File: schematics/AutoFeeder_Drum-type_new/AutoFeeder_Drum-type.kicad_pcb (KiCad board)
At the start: 2 copper layers, 68.5 x 80 mm, 58 parts, among them J1 USB_C_Receptacle_6, J2 Conn_01x04, J3 Conn_01x05, J4 Conn_02x02_Odd_Even, J5 Conn_01x04, J6 Conn_01x02, J7 Conn_01x04, J8 Conn_01x03, J9 Conn_01x04, M1 Motor_DC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

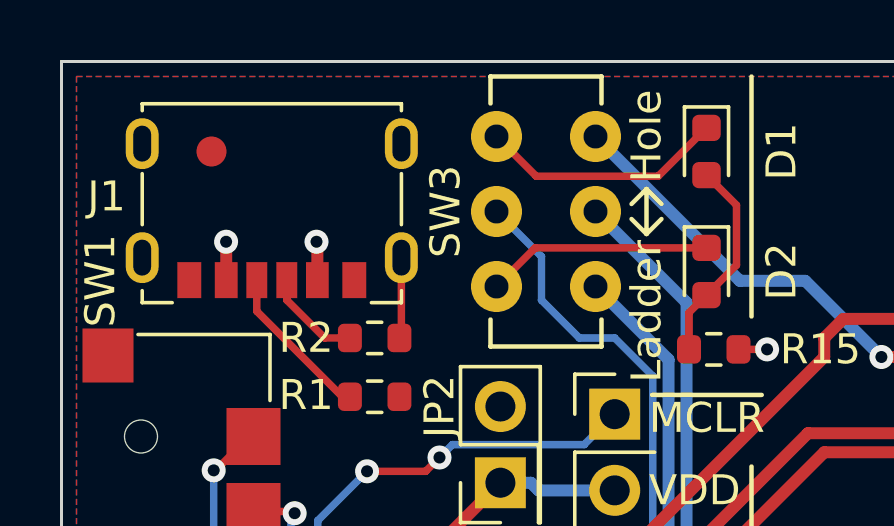
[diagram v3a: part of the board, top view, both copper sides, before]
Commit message: PCB modification: Slightly lengthened the pins of the USB Type-C connector to improve solderability.
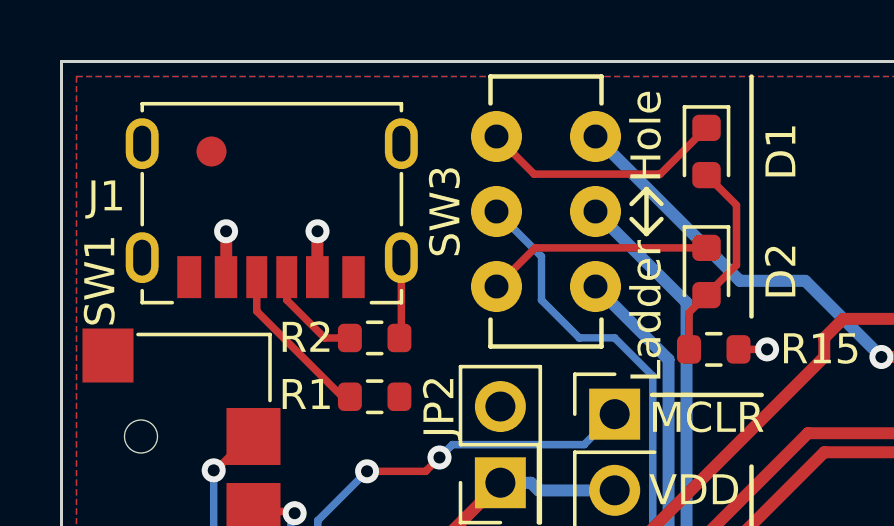
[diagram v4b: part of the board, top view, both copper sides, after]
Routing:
- net +5V: track 49.1 -> 49.8 mm
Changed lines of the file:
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@@
   (net 4 "Net-(J1-PadA5)")
   (net 5 "Net-(J1-PadB5)")
-  (net 6 "Net-(SW3-Pad4)")
+  (net 6 "Net-(D1-Pad1)")
   (net 7 "Net-(D1-Pad2)")
   (net 8 "/Sensor0")
@@
   (net 32 "unconnected-(SW2-Pad5)")
   (net 33 "unconnected-(SW2-Pad6)")
-  (net 34 "Net-(SW3-Pad6)")
+  (net 34 "Net-(D2-Pad1)")
   (net 35 "Net-(J3-Pad4)")
   (net 36 "unconnected-(U1-Pad3)")
@@
     (fp_line (start 4.9 -5.4) (end 4.9 2.6) (layer "F.CrtYd") (width 0.05))
     (fp_line (start 4.9 2.6) (end -4.9 2.6) (layer "F.CrtYd") (width 0.05))
-    (pad "A5" smd rect (at -0.5 -4.55 270) (size 1.2 0.7) (layers "F.Cu" "F.Paste" "F.Mask")
+    (pad "A5" smd rect (at -0.5 -4.45 270) (size 1.4 0.7) (layers "F.Cu" "F.Paste" "F.Mask")
       (net 4 "Net-(J1-PadA5)") (pinfunction "CC1") (pintype "bidirectional"))
-    (pad "A9" smd rect (at 1.52 -4.55 270) (size 1.2 0.76) (layers "F.Cu" "F.Paste" "F.Mask")
+    (pad "A9" smd rect (at 1.525 -4.45 270) (size 1.4 0.75) (layers "F.Cu" "F.Paste" "F.Mask")
       (net 2 "+5V") (pinfunction "VBUS") (pintype "passive"))
-    (pad "A12" smd rect (at 2.75 -4.55 270) (size 1.2 0.8) (layers "F.Cu" "F.Paste" "F.Mask")
+    (pad "A12" smd rect (at 2.75 -4.45 270) (size 1.4 0.8) (layers "F.Cu" "F.Paste" "F.Mask")
       (net 1 "GND") (pinfunction "GND") (pintype "passive"))
-    (pad "B5" smd rect (at 0.5 -4.55 270) (size 1.2 0.7) (layers "F.Cu" "F.Paste" "F.Mask")
+    (pad "B5" smd rect (at 0.5 -4.45 270) (size 1.4 0.7) (layers "F.Cu" "F.Paste" "F.Mask")
       (net 5 "Net-(J1-PadB5)") (pinfunction "CC2") (pintype "bidirectional"))
-    (pad "B9" smd rect (at -1.52 -4.55 270) (size 1.2 0.76) (layers "F.Cu" "F.Paste" "F.Mask")
+    (pad "B9" smd rect (at -1.52 -4.45 270) (size 1.4 0.76) (layers "F.Cu" "F.Paste" "F.Mask")
       (net 2 "+5V") (pinfunction "VBUS") (pintype "passive"))
-    (pad "B12" smd rect (at -2.75 -4.55 270) (size 1.2 0.8) (layers "F.Cu" "F.Paste" "F.Mask")
+    (pad "B12" smd rect (at -2.725 -4.45 270) (size 1.4 0.75) (layers "F.Cu" "F.Paste" "F.Mask")
       (net 1 "GND") (pinfunction "GND") (pintype "passive"))
     (pad "S1" thru_hole oval (at 4.32 -3.8 270) (size 1.7 1.1) (drill oval 1.2 0.6) (layers *.Cu *.Mask)
@@
     (fp_line (start 0.8 -0.4) (end -0.5 -0.4) (layer "F.Fab") (width 0.1))
     (pad "1" smd roundrect (at -0.7875 0 270) (size 0.875 0.95) (layers "F.Cu" "F.Paste" "F.Mask") (roundrect_rratio 0.25)
-      (net 34 "Net-(SW3-Pad6)") (pinfunction "K") (pintype "passive"))
+      (net 34 "Net-(D2-Pad1)") (pinfunction "K") (pintype "passive"))
     (pad "2" smd roundrect (at 0.7875 0 270) (size 0.875 0.95) (layers "F.Cu" "F.Paste" "F.Mask") (roundrect_rratio 0.25)
       (net 7 "Net-(D1-Pad2)") (pinfunction "A") (pintype "passive"))
@@
     (fp_line (start 0.8 0.4) (end 0.8 -0.4) (layer "F.Fab") (width 0.1))
     (pad "1" smd roundrect (at -0.7875 0 270) (size 0.875 0.95) (layers "F.Cu" "F.Paste" "F.Mask") (roundrect_rratio 0.25)
-      (net 6 "Net-(SW3-Pad4)") (pinfunction "K") (pintype "passive"))
+      (net 6 "Net-(D1-Pad1)") (pinfunction "K") (pintype "passive"))
     (pad "2" smd roundrect (at 0.7875 0 270) (size 0.875 0.95) (layers "F.Cu" "F.Paste" "F.Mask") (roundrect_rratio 0.25)
       (net 7 "Net-(D1-Pad2)") (pinfunction "A") (pintype "passive"))
@@
       (net 14 "/Sensor1") (pinfunction "C") (pintype "passive"))
     (pad "4" thru_hole circle locked (at 0 3.3 270) (size 1.7 1.7) (drill 0.8) (layers *.Cu *.Mask)
-      (net 6 "Net-(SW3-Pad4)") (pinfunction "A") (pintype "passive"))
+      (net 6 "Net-(D1-Pad1)") (pinfunction "A") (pintype "passive"))
     (pad "5" thru_hole circle locked (at 2.5 3.3 270) (size 1.7 1.7) (drill 0.8) (layers *.Cu *.Mask)
       (net 35 "Net-(J3-Pad4)") (pinfunction "B") (pintype "passive"))
     (pad "6" thru_hole circle locked (at 5 3.3 270) (size 1.7 1.7) (drill 0.8) (layers *.Cu *.Mask)
-      (net 34 "Net-(SW3-Pad6)") (pinfunction "C") (pintype "passive"))
+      (net 34 "Net-(D2-Pad1)") (pinfunction "C") (pintype "passive"))
   )
   (footprint "Resistor_SMD:R_0603_1608Metric" (layer "F.Cu")
@@
   (segment (start 176.5 109.8) (end 176.2 109.8) (width 0.25) (layer "B.Cu") (net 1))
   (segment (start 176.2 109.8) (end 175 111) (width 0.25) (layer "B.Cu") (net 1))
-  (segment (start 141.99 66.012) (end 141.99 67.288) (width 0.4) (layer "F.Cu") (net 2))
+  (segment (start 145.034 65.659) (end 145.03 65.663) (width 0.4) (layer "F.Cu") (net 2))
   (segment (start 156.4 98.425) (end 155.765 97.79) (width 0.25) (layer "F.Cu") (net 2))
+  (segment (start 145.03 65.663) (end 145.03 67.288) (width 0.4) (layer "F.Cu") (net 2))
   (segment (start 156.718 117.983) (end 155.478 117.983) (width 0.4) (layer "F.Cu") (net 2))
   (segment (start 185.98 68.505) (end 186.88 69.405) (width 0.4) (layer "F.Cu") (net 2))
@@
   (segment (start 185.98 61.585) (end 185.98 68.505) (width 0.25) (layer "F.Cu") (net 2))
   (segment (start 186.88 69.405) (end 186.88 73) (width 0.4) (layer "F.Cu") (net 2))
-  (segment (start 145 66.008) (end 145.03 66.038) (width 0.4) (layer "F.Cu") (net 2))
   (segment (start 156.21 100.19) (end 155.38 100.19) (width 0.25) (layer "F.Cu") (net 2))
   (segment (start 186.215 61.35) (end 185.98 61.585) (width 0.25) (layer "F.Cu") (net 2))
@@
   (segment (start 155.38 100.19) (end 155.38 104.5) (width 0.25) (layer "F.Cu") (net 2))
   (segment (start 156.591 98.425) (end 156.21 98.806) (width 0.25) (layer "F.Cu") (net 2))
-  (segment (start 145.03 66.038) (end 145.03 67.288) (width 0.4) (layer "F.Cu") (net 2))
+  (segment (start 141.986 65.659) (end 141.99 65.663) (width 0.4) (layer "F.Cu") (net 2))
   (segment (start 186.63 61.35) (end 186.215 61.35) (width 0.25) (layer "F.Cu") (net 2))
   (segment (start 156.21 98.806) (end 156.21 100.19) (width 0.25) (layer "F.Cu") (net 2))
   (segment (start 160.02 69.596) (end 159.067 69.596) (width 0.25) (layer "F.Cu") (net 2))
+  (segment (start 141.99 65.663) (end 141.99 67.288) (width 0.4) (layer "F.Cu") (net 2))
   (segment (start 181.685 68.505) (end 185.98 68.505) (width 0.25) (layer "F.Cu") (net 2))
-  (segment (start 141.986 66.008) (end 141.99 66.012) (width 0.4) (layer "F.Cu") (net 2))
   (segment (start 187.185 76) (end 186.88 75.695) (width 0.4) (layer "F.Cu") (net 2))
   (via (at 156.718 117.983) (size 0.8) (drill 0.4) (layers "F.Cu" "B.Cu") (net 2))
@@
   (via (at 181.685 68.505) (size 0.8) (drill 0.4) (layers "F.Cu" "B.Cu") (net 2))
   (via (at 160.02 69.596) (size 0.8) (drill 0.4) (layers "F.Cu" "B.Cu") (net 2))
-  (via (at 145 66.008) (size 0.8) (drill 0.4) (layers "F.Cu" "B.Cu") (net 2))
-  (via (at 141.986 66.008) (size 0.8) (drill 0.4) (layers "F.Cu" "B.Cu") (net 2))
+  (via (at 145.034 65.659) (size 0.8) (drill 0.4) (layers "F.Cu" "B.Cu") (net 2))
+  (via (at 141.986 65.659) (size 0.8) (drill 0.4) (layers "F.Cu" "B.Cu") (net 2))
   (segment (start 176.5 68.5) (end 181.68 68.5) (width 0.25) (layer "B.Cu") (net 2))
   (segment (start 176.5 78) (end 176.5 68.5) (width 0.25) (layer "B.Cu") (net 2))
@@
   (segment (start 145.86 71.175) (end 143.01 68.325) (width 0.25) (layer "F.Cu") (net 5))
   (segment (start 143.01 68.325) (end 143.01 67.288) (width 0.25) (layer "F.Cu") (net 5))
-  (segment (start 152.325 63.825) (end 156.3875 63.825) (width 0.25) (layer "F.Cu") (net 6))
-  (segment (start 156.3875 63.825) (end 158 62.2125) (width 0.25) (layer "F.Cu") (net 6))
-  (segment (start 151 62.5) (end 152.325 63.825) (width 0.25) (layer "F.Cu") (net 6))
+  (segment (start 151 62.5) (end 152.254 63.754) (width 0.25) (layer "F.Cu") (net 6))
+  (segment (start 152.254 63.754) (end 156.4585 63.754) (width 0.25) (layer "F.Cu") (net 6))
+  (segment (start 156.4585 63.754) (end 158 62.2125) (width 0.25) (layer "F.Cu") (net 6))
   (segment (start 157.417 68.3705) (end 157.417 69.596) (width 0.25) (layer "F.Cu") (net 7))
   (segment (start 159 64.7875) (end 159 66.7875) (width 0.25) (layer "F.Cu") (net 7))
@@
   (via (at 141.573397 73.628797) (size 0.8) (drill 0.4) (layers "F.Cu" "B.Cu") (net 30))
   (segment (start 141.573397 83.915397) (end 141.573397 73.628797) (width 0.25) (layer "B.Cu") (net 30))
+  (segment (start 151 67.5) (end 152.2875 66.2125) (width 0.25) (layer "F.Cu") (net 34))
   (segment (start 152.2875 66.2125) (end 158 66.2125) (width 0.25) (layer "F.Cu") (net 34))
-  (segment (start 151 67.5) (end 152.2875 66.2125) (width 0.25) (layer "F.Cu") (net 34))
   (segment (start 151.7 80.645) (end 153.035 80.645) (width 0.25) (layer "F.Cu") (net 35))
   (segment (start 154.305 79.375) (end 154.94 79.375) (width 0.25) (layer "F.Cu") (net 35))

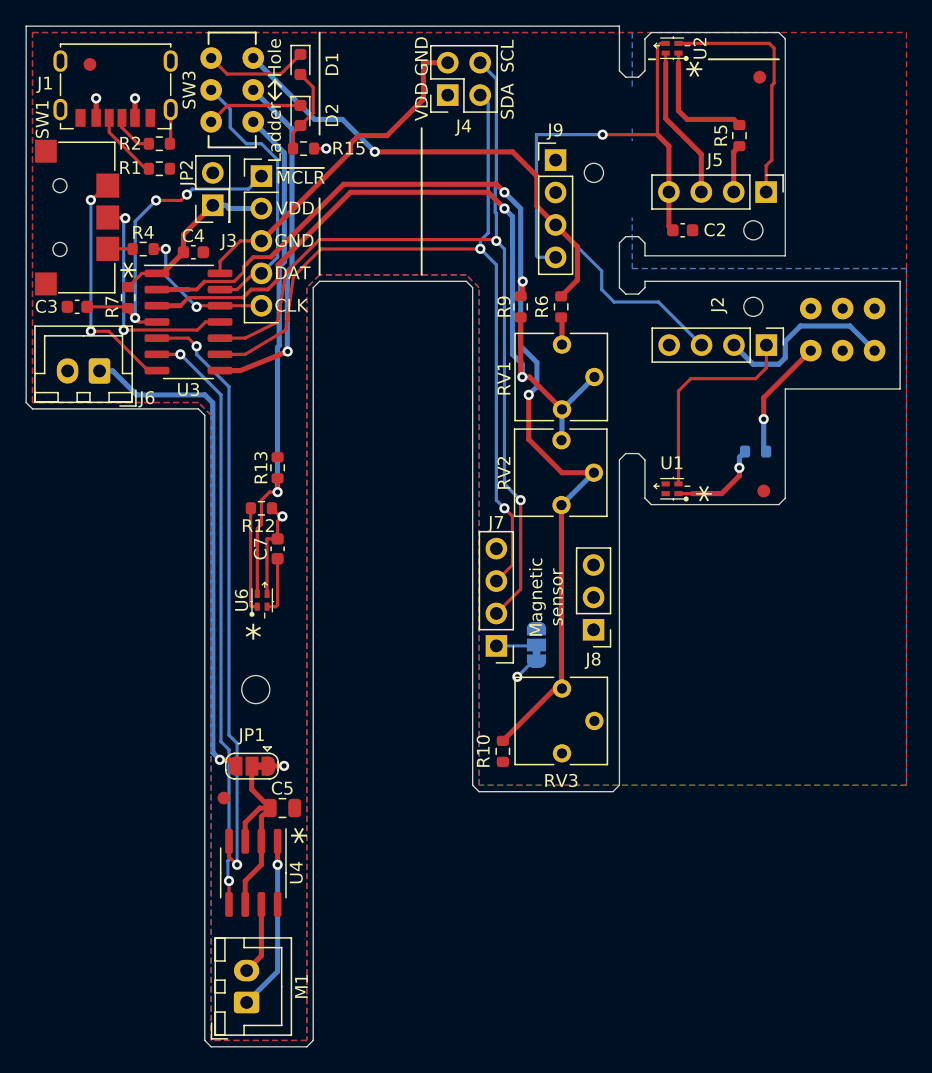
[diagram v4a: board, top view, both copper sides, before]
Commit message: Change schematics: Assign CW/CCW pin to connector; Add M3 mounting hole
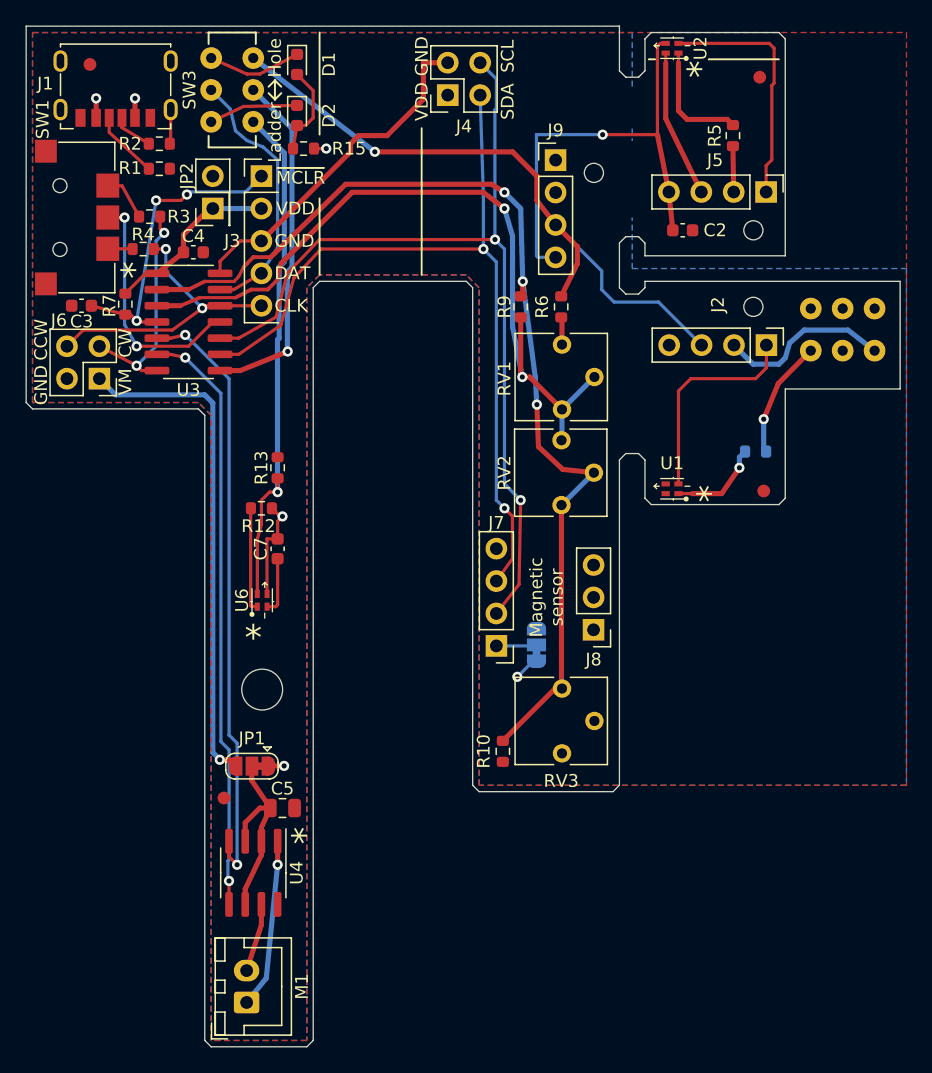
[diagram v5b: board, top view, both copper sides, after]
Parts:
- removed the REF** at (154.5, 112.0)
- added R3: 1k, Resistor_SMD:R_0603_1608Metric, F.Cu at (146.2, 74.9)
- added REF**: MountingHole_3.2mm_M3_DIN965, MountingHole:MountingHole_3.2mm_M3_DIN965, F.Cu at (155.0, 112.0)
- J6: value Conn_01x02 -> Conn_02x02_Odd_Even; footprint Connector_JST:JST_XH_B2B-XH-A_1x02_P2.50mm_Vertical -> Connector_PinHeader_2.54mm:PinHeader_2x02_P2.54mm_Vertical
- moved J6 0.61 mm to (142.2, 87.6)
- moved R7 0.56 mm to (144.3, 81.8)
- moved R5 0.51 mm to (191.9, 68.6)
- moved C3 0.35 mm to (140.8, 81.9)
- moved D1 0.27 mm to (157.7, 63.0)
- moved D2 0.27 mm to (157.7, 67.0)
- moved JP2 0.25 mm to (151.1, 74.3)
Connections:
- SW1 pad 2: /CW -> Net-(R3-Pad1)
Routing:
- net /CCW: track 11.6 -> 23.2 mm
- net Net-(R3-Pad1): track 0.00 -> 3.88 mm
- net /RA5: track 83.7 -> 81.9 mm
- net /SDA: track 65.6 -> 64.6 mm
- net Net-(C3-Pad1): track 25.0 -> 24.1 mm
- net /RA2: track 18.0 -> 19.0 mm
- net /RA4: track 60.8 -> 59.9 mm
- net /Sensor0: track 53.5 -> 52.6 mm
- net /CW: track 18.6 -> 17.8 mm
- net Net-(J2-Pad2): track 14.4 -> 13.7 mm
- net Net-(D1-Pad1): track 8.16 -> 7.38 mm
- net Net-(J3-Pad4): track 21.5 -> 20.8 mm
- net /SCL: track 71.7 -> 71.0 mm
- net Net-(C5-Pad1): track 16.2 -> 15.7 mm
- net Net-(D2-Pad1): track 7.53 -> 7.01 mm
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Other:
- board text added: "CCW"
- board text added: "CW"
- board text added: "VM"

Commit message: Schematics: Add +5V to J6; Fine-tuning of patterns
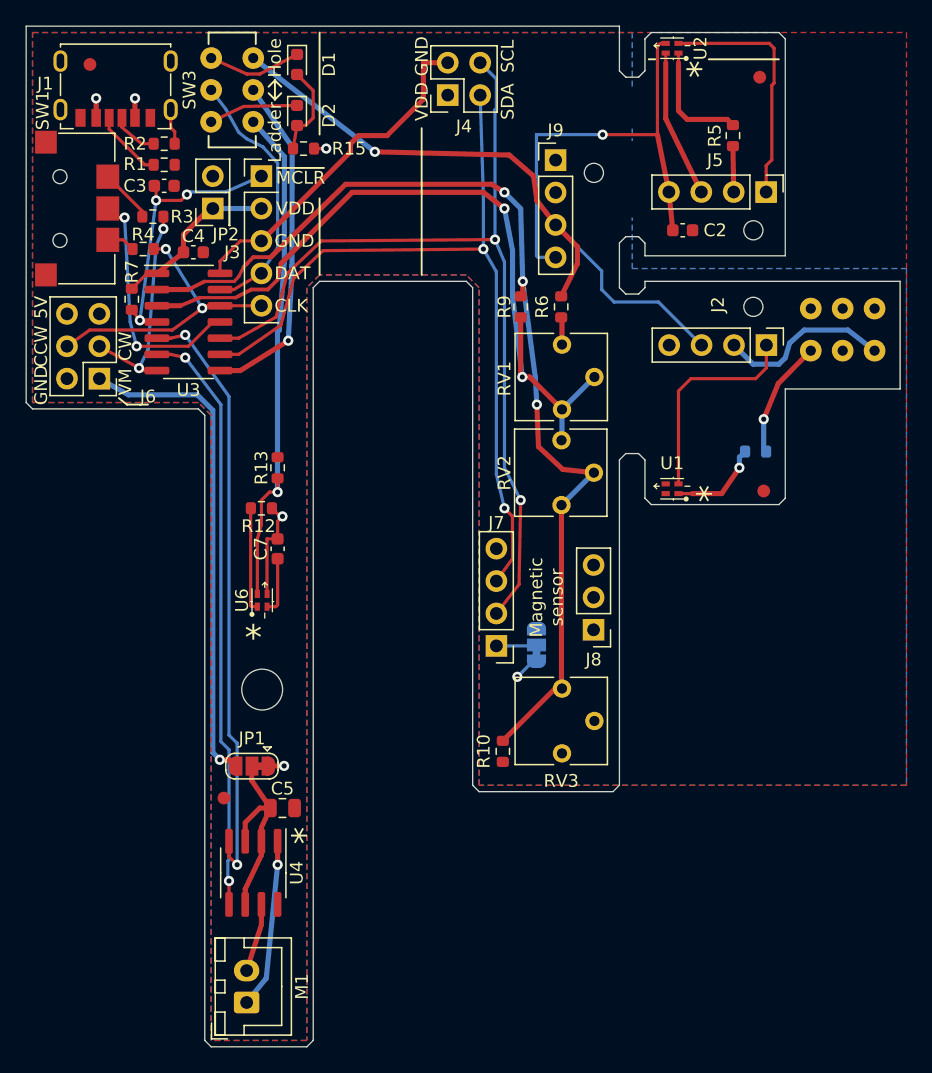
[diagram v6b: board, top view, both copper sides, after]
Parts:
- J6: value Conn_02x02_Odd_Even -> Conn_02x03_Odd_Even; footprint Connector_PinHeader_2.54mm:PinHeader_2x02_P2.54mm_Vertical -> Connector_PinHeader_2.54mm:PinHeader_2x03_P2.54mm_Vertical
- moved C3 11.4 mm to (147.3, 72.5), turned to 0 degrees
- moved SW1 0.70 mm to (139.3, 74.3)
- moved R7 0.64 mm to (144.8, 81.4)
- moved R1 0.49 mm to (147.3, 70.9)
- moved R2 0.38 mm to (147.3, 69.2)
- moved R3 0.25 mm to (146.4, 74.9)
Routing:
- net Net-(C3-Pad1): track 24.1 -> 22.2 mm
- net Net-(C4-Pad2): track 14.1 -> 13.5 mm
- net Net-(SW3-Pad2): track 27.5 -> 26.9 mm
- net /CW: track 17.8 -> 17.2 mm
- net Net-(JP1-Pad3): track 39.3 -> 38.8 mm
- net /SCL: track 71.0 -> 70.5 mm
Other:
- board text added: "5V"
- board text removed: "0.25mm Not required"

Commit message: Schematics: Add Diode OR (D3 and D4) for manual feed and auto feed
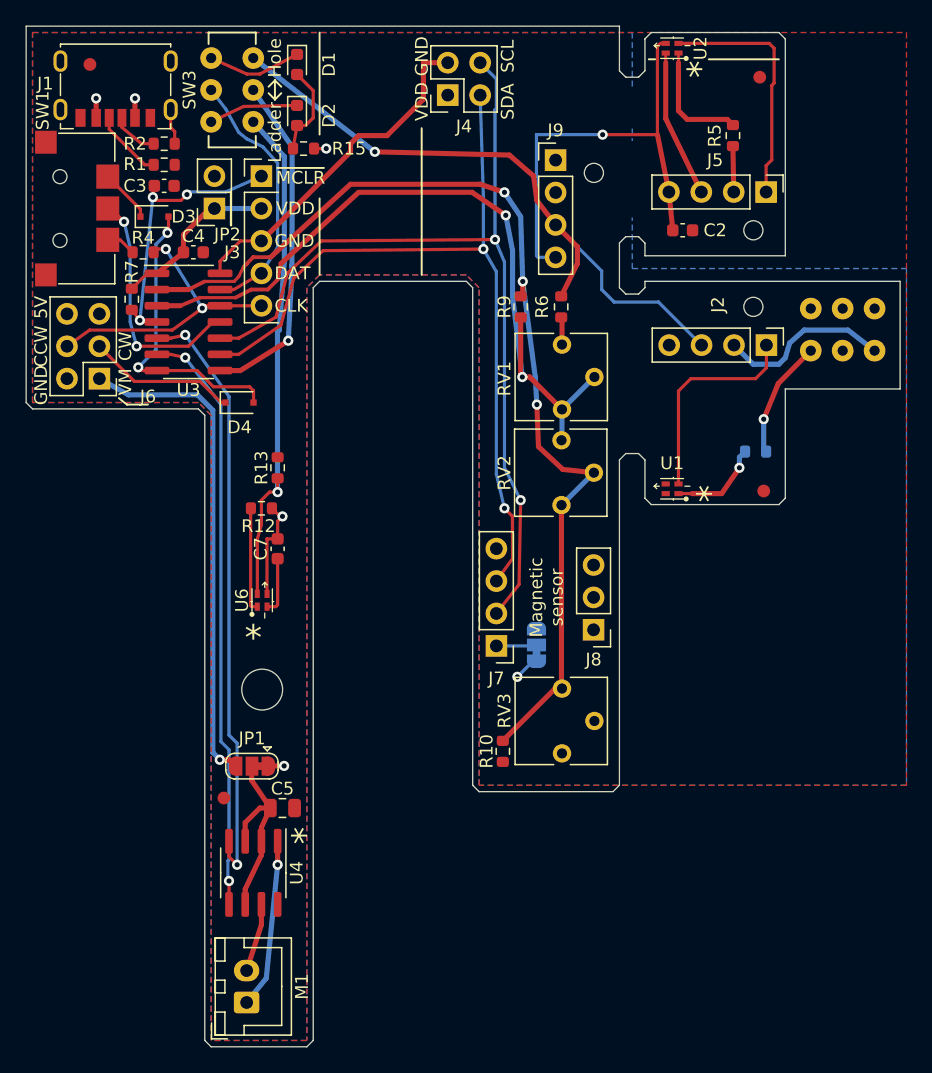
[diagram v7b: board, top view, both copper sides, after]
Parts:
- removed R3: 1k, Resistor_SMD:R_0603_1608Metric
- added D3: 1SS355VM, Diode_SMD:D_SOD-323F, F.Cu at (146.6, 74.9)
- added D4: 1SS355VM, Diode_SMD:D_SOD-323F, F.Cu at (153.2, 89.5)
- moved R4 0.25 mm to (145.7, 77.7)
- moved JP2 0.13 mm to (151.3, 74.3)
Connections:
- J6 pad 3: /CW -> Net-(D4-Pad1)
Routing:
- net Net-(D4-Pad1): track 0.00 -> 11.7 mm
- net /CW: track 17.2 -> 23.5 mm
